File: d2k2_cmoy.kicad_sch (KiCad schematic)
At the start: 23 parts, among them J1 Jack_3.5mm_3pin, J2 Jack_3.5mm_3pin, SW1 SPST, U1 MC33178

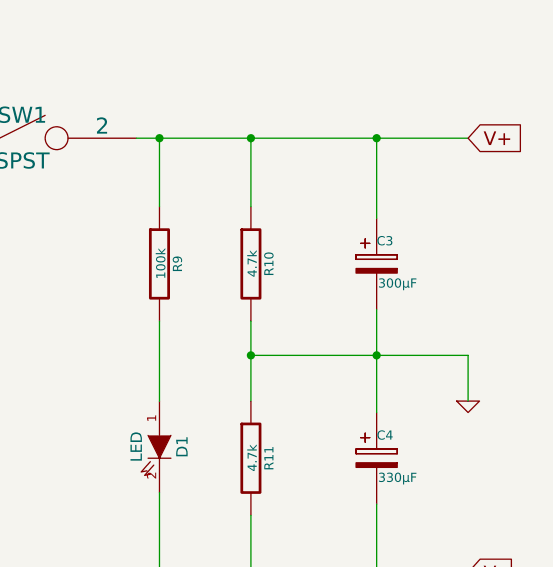
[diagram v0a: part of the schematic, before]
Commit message: typo fix, C3 and C4 are 330uF
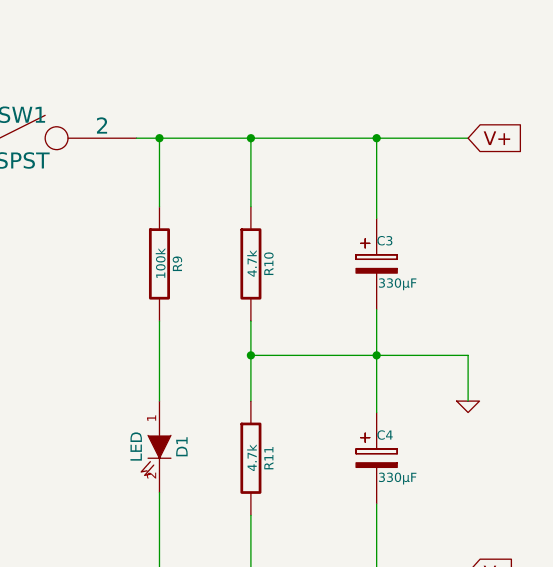
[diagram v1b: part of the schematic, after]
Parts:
- C3: value 300µF -> 330µF
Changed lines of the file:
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@@
       (effects (font (size 1.016 1.016)) (justify left))
     )
-    (property "Value" "300µF" (id 1) (at 259.2324 122.809 0)
+    (property "Value" "330µF" (id 1) (at 259.2324 122.809 0)
       (effects (font (size 1.016 1.016)) (justify left))
     )
@@
     )
     (path "/00000000-0000-0000-0000-0000552bb266"
-      (reference "C3") (unit 1) (value "300µF") (footprint "")
+      (reference "C3") (unit 1) (value "330µF") (footprint "")
     )
     (path "/00000000-0000-0000-0000-0000552bb2b3"
